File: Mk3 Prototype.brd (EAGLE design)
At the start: 113 x 53.5 mm, 133 parts, among them IC1 STM32F401R, IC2 CC3100, IC3 S25FL216K0PMFI011, J1 ZX62-AB-5PA(11), J2 SWD_SHROUD_SMD, J4 Arduino Headers, J7 SFV30R-2STE1HLF, Q1 BSS84W, Q10 2N7002KW, Q11 BSS84W, Q12 2N7002KW, U1 USD-SOCKETNEW, U2 JHD12864-G13BSW-OUTLINE, U3 MCP73831, X1 ABS07-32.768KHZ-T, X2 Q24FA20H00396, X3 CRYSTAL-3.2-2.5, X4 ABS07-32.768KHZ-T, Y1 AH316M245001-T

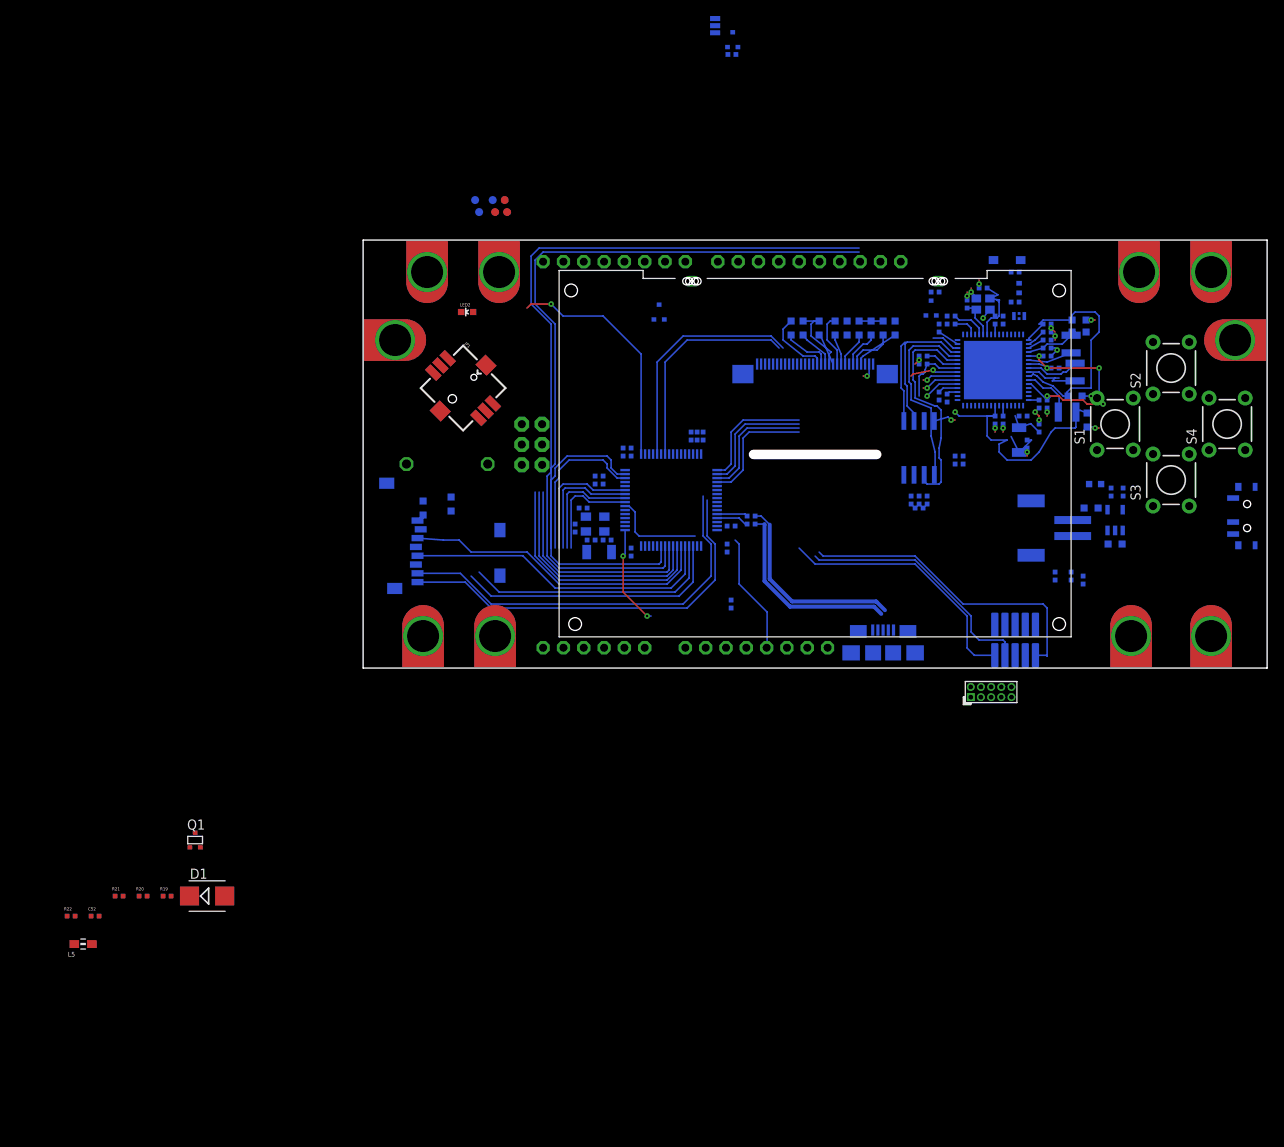
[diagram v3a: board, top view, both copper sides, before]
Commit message: starting stm32 100pin schematic
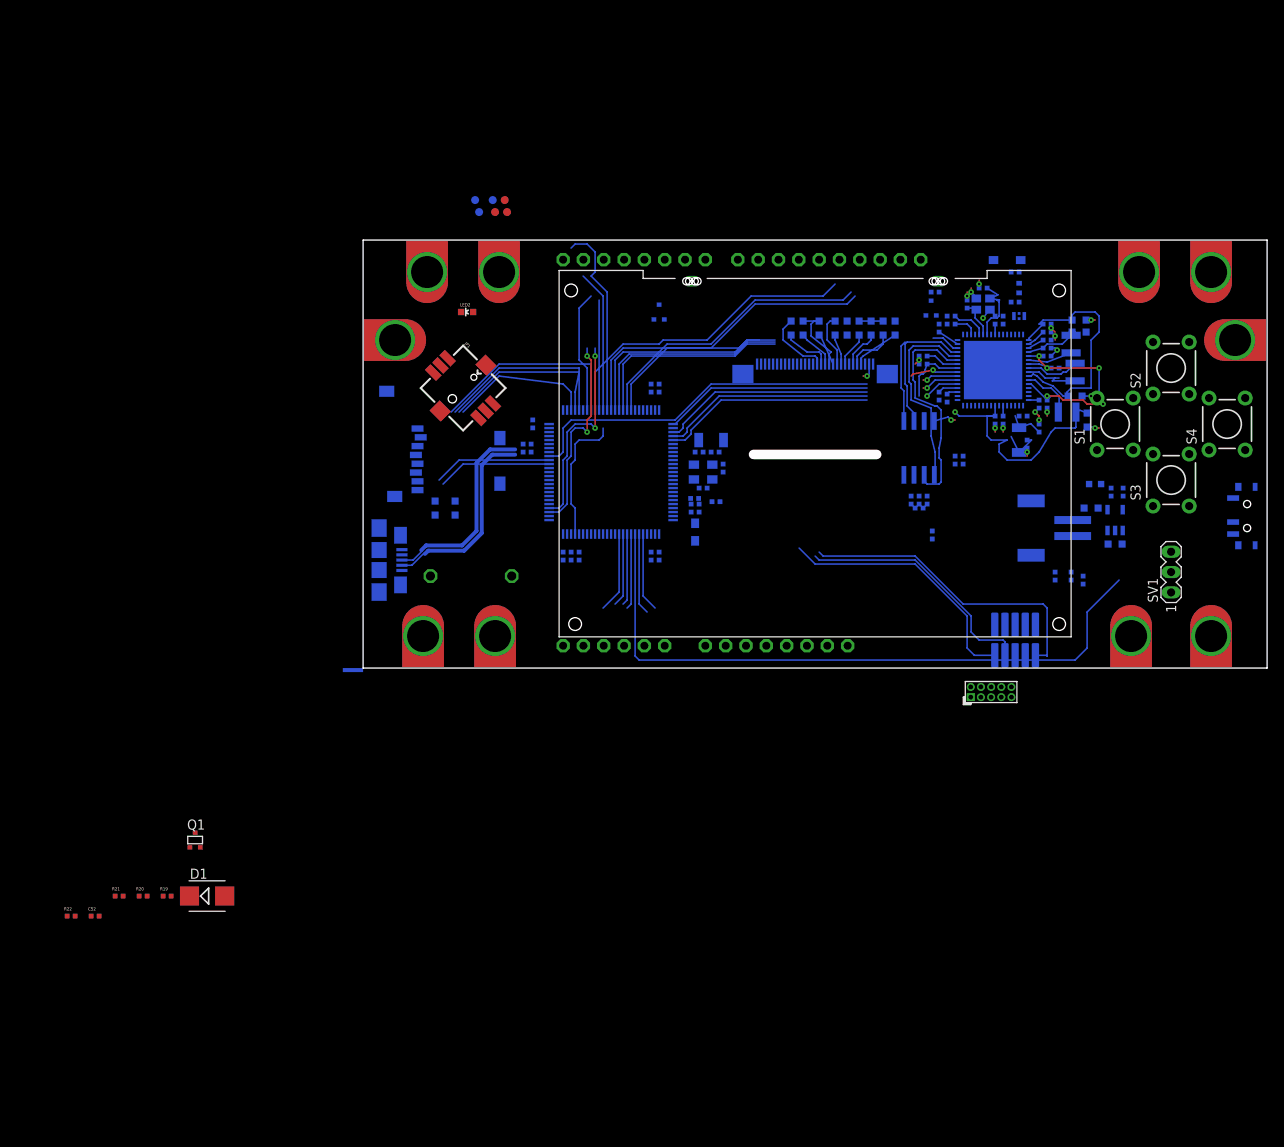
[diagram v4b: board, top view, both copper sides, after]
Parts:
- removed IC1: STM32F401R, TiLDA Mk3 Parts:LQFP64-10X10
- removed J4: Arduino Headers, TiLDA Mk3 Parts:ARDUINOR3-LWKTXT-REF-SPI
- removed Q10: 2N7002KW, TiLDA Mk3 Parts:SC70-3-R
- removed R42: 0402/10K/5%, TiLDA Mk3 Parts:R0402-SMALLER
- removed SJ3: ISP_RESET, TiLDA Mk3 Parts:SJ_3
- added C55: 0402/1u/10V/X5R, TiLDA Mk3 Parts:C0402-SMALLER
- added C56: 0402/100n/10V/X5R, TiLDA Mk3 Parts:C0402-SMALLER
- added IC4: STM32F401V, TiLDA Mk3 Parts:TQFP100
- added SV1: (no value), con-lstb:MA03-1
- added U4: ARDUINOR3-NODIM, TiLDA Mk3 Parts:ARDUINOR3-NODIM
- C49: value 0402/0R -> 0402/100n/10V/X5R
- moved L5 92.2 mm to (41.5, 17.0), flipped to the bottom, turned to 90 degrees
- moved J1 64.1 mm to (2.00, 13.5), turned to 180 degrees
- moved R16 29.7 mm to (20.5, 28.0), turned to 0 degrees
- moved R15 29.1 mm to (20.5, 27.0), turned to 0 degrees
- moved R14 26.6 mm to (71.1, 16.6)
- moved C7 23.0 mm to (25.0, 14.0), turned to 90 degrees
- moved C9 22.4 mm to (36.5, 35.5), turned to 180 degrees
- moved C10 20.5 mm to (27.0, 14.0)
- moved C48 20.3 mm to (26.0, 14.0), turned to 90 degrees
- moved C5 20.2 mm to (36.5, 34.5), turned to 180 degrees
- moved C35 20.0 mm to (45.0, 25.0)
- moved X4 19.8 mm to (43.5, 28.5)
- moved C53 19.0 mm to (44.0, 27.0), turned to 180 degrees
- moved C54 15.9 mm to (42.0, 27.0), turned to 180 degrees
- moved C36 15.2 mm to (42.5, 22.5), turned to 0 degrees
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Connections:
- removed net D10: J4.D10
- removed net D11: J4.D11
- removed net D12: J4.D12
- removed net D13: J4.D13
- removed net D5: J4.D5
- removed net D6: J4.D6
- removed net D9: J4.D9
- removed net ISP_!RESET: J4.!RESET@ISP, Q10.3, SJ3.1, SJ3.2
- removed net ISP_!RESET!_IO: Q10.1, R42.1
- removed net N$39: IC1.22
- removed net N$42: IC1.26
- removed net N$43: IC1.24
- removed net N$44: IC1.62
- removed net N$45: IC1.25
- removed net N$49: IC1.16
- removed net N$50: IC1.50
- removed net N$51: IC1.27
- removed net N$53: IC1.61
- removed net N$54: IC1.29
- removed net RX: J4.D0
- removed net SPI1_CLK: IC1.21, J7.13
- removed net SPI3_MISO: IC1.56, J4.MISO
- removed net TX: J4.D1
- removed net WIFI_CLK: IC1.34, IC2.5
- removed net WIFI_CS: IC1.33, IC2.8
- removed net WIFI_MISO: IC1.35, IC2.7
- removed net WIFI_MOSI: IC1.36, IC2.6
- new net SPI2_CLK: IC4.84, U4.D13
- new net SPI2_MISO: IC4.53, U4.D12
- new net SPI2_MOSI: IC4.54, U4.D11
- new net SPI4_MISO: IC2.7, IC4.4
- new net SPI4_MOSI: IC2.6, IC4.5
- new net SPI4_NSS: IC2.8, IC4.3
- new net SPI4_SCK: IC2.5, IC4.1
- new net TIM2_CH1: IC4.77, U4.D6
- new net TIM2_CH3: IC4.47, U4.D5
- new net TIM4_CH3: IC4.95, U4.D9
- new net TIM4_CH4: IC4.96, U4.D10
- new net USART2_RX: IC4.87, U4.D0
- new net USART2_TX: IC4.86, U4.D1
- net +3V3: now also C49.2, C56.2, IC4.100, IC4.11, IC4.19, IC4.28, IC4.50, IC4.75, U4.3V, U4.IOREF; no longer IC1.19, IC1.32, IC1.48, IC1.64, J4.3V, J4.IOREF
- net 5V0: now also U4.5V; no longer J4.5V, J4.5V@ISP
- net A0: now also IC4.30, U4.A0; no longer IC1.8, J4.A0
- net A1: now also IC4.31, U4.A1; no longer IC1.9, J4.A1
- net A2: now also IC4.33, U4.A2; no longer IC1.10, J4.A2
- net A3: now also IC4.34, U4.A3; no longer IC1.11, J4.A3
- net A4: now also IC4.35, U4.A4; no longer IC1.14, J4.A4
- net A5: now also IC4.36, U4.A5; no longer IC1.15, J4.A5
- net ADC3: now also IC4.26; no longer IC1.17
- net AREF: now also U4.AREF; no longer J4.AREF
- net BOOT0: now also IC4.94; no longer IC1.60
- net D2: now also IC4.82, U4.D2; no longer J4.D2
- net D3: now also U4.D3; no longer J4.D3
- net D4: now also IC4.85, U4.D4; no longer J4.D4
- net D7: now also IC4.98, U4.D7; no longer J4.D7
- net D8: now also IC4.97, U4.D8; no longer J4.D8
- net D_N: now also IC4.70; no longer IC1.44
- net D_P: now also IC4.71; no longer IC1.45
- net GND: now also C55.1, C56.1, IC4.10, IC4.20, IC4.27, IC4.74, IC4.99, U4.GND, U4.GND1, U4.GND2; no longer IC1.12, IC1.18, IC1.63, J4.GND@1, J4.GND@2, J4.GND@3, J4.GND@ISP, Q10.2, R42.2
- net I2C_SCL: now also IC4.92, U4.SCL; no longer IC1.58, J4.SCL
- net I2C_SDA: now also IC4.93, U4.SDA; no longer IC1.59, J4.SDA
- net LCD_!CS: now also IC4.90
- net LCD_A0: now also IC4.88
- net MASTER_RESET: now also U4.RESET; no longer J4.!RESET, SJ3.3
- net MCO1: now also IC4.67; no longer IC1.41
- net N$13: now also IC4.21, IC4.22; no longer IC1.13
- net N$30: now also IC4.69; no longer IC1.43
- net N$31: now also IC4.12; no longer IC1.5
- net N$32: now also IC4.68; no longer IC1.42
- net N$33: now also IC4.13; no longer IC1.6
- net N$37: now also IC4.49; no longer IC1.47
- net N$38: now also C55.2, IC4.73; no longer C49.2, IC1.31
- net N$4: now also IC4.48; no longer IC1.30
- net N$48: now also IC4.29; no longer IC1.20
- net N$52: now also IC4.37; no longer IC1.28
- net N$55: now also IC4.63; no longer IC1.37
- net N$56: now also IC4.64; no longer IC1.38
- net NRST: now also IC4.14; no longer IC1.7
- net OCS32_IN: now also IC4.8; no longer IC1.3
- net OCS32_OUT: now also IC4.9; no longer IC1.4
- net SDIO_CLK: now also IC4.80; no longer IC1.53
- net SDIO_CMD: now also IC4.83; no longer IC1.54
- net SDIO_D0: now also IC4.65; no longer IC1.39
- net SDIO_D1: now also IC4.66; no longer IC1.40
- net SDIO_D2: now also IC4.78; no longer IC1.51
- net SDIO_D3: now also IC4.79; no longer IC1.52
- net SDIO_SW: now also IC4.7; no longer IC1.2
- net SPI1_MOSI: now also IC4.32, SV1.2; no longer IC1.23, J7.14
- net SPI3_MOSI: now also IC4.91, J7.14; no longer IC1.57, J4.MOSI
- net SPI3_SCK: now also IC4.89, J7.13; no longer IC1.55, J4.SCK
- net SWCLK: now also IC4.76; no longer IC1.49
- net SWDAT: now also IC4.72; no longer IC1.46
- net VBATT_IN: now also IC4.6; no longer IC1.1
- net VIN: now also U4.VIN; no longer J4.VIN
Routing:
- net I2C_SCL: track 98.1 -> 36.0 mm
- net I2C_SDA: track 95.4 -> 35.8 mm
- net SPI1_MOSI: track 27.3 -> 82.7 mm
- net MCO1: track 0.00 -> 45.2 mm
- net SPI2_CLK: track 0.00 -> 39.3 mm
- net SDIO_D0: track 50.2 -> 14.3 mm
- net SDIO_D1: track 50.4 -> 14.8 mm
- net SPI4_NSS: track 0.00 -> 32.7 mm, vias 0 -> 1
- net SPI4_MOSI: track 0.00 -> 31.3 mm, vias 0 -> 1
- net SPI4_MISO: track 0.00 -> 31.1 mm, vias 0 -> 1
- net SPI4_SCK: track 0.00 -> 30.5 mm, vias 0 -> 1
- net ADC3: track 29.5 -> 0.00 mm, vias 1 -> 0
- net SPI1_CLK: track 29.2 -> 0.00 mm
- net SPI3_MISO: track 29.1 -> 0.00 mm
- net LCD_!CS: track 0.00 -> 26.4 mm
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
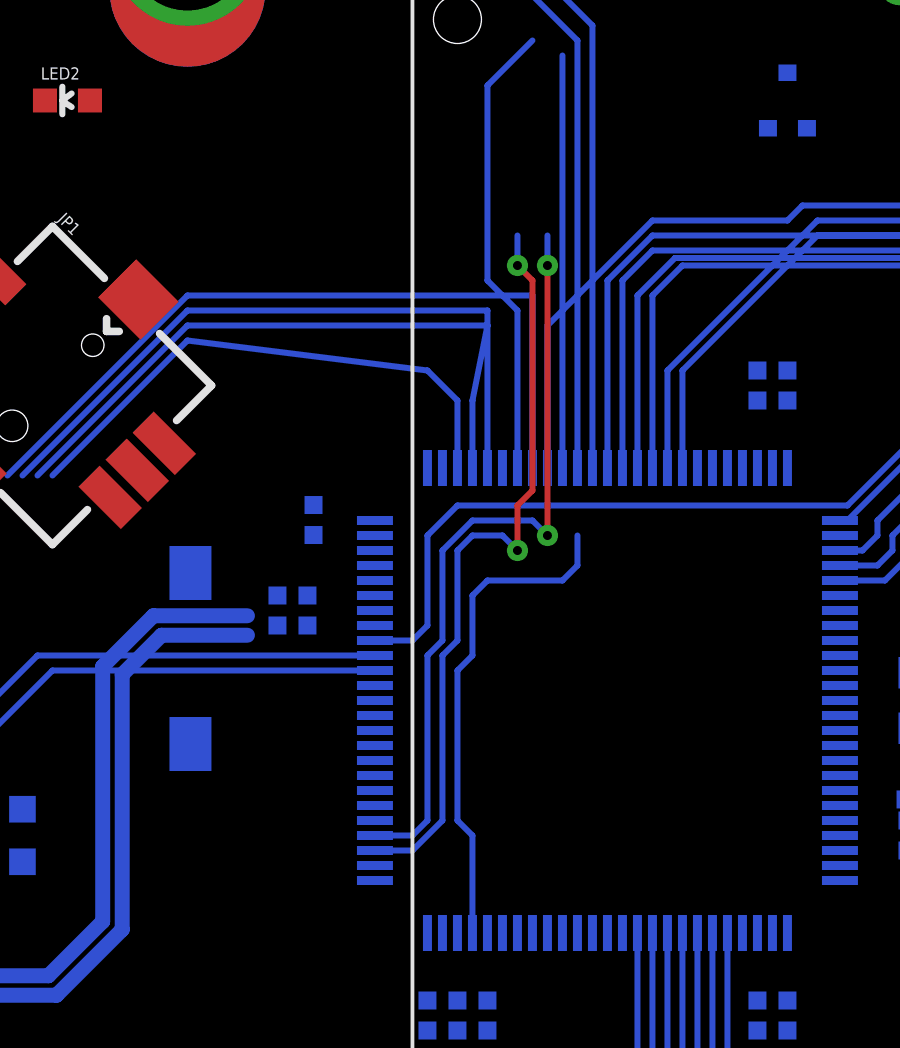
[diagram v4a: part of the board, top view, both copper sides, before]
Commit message: arduino gpio wired
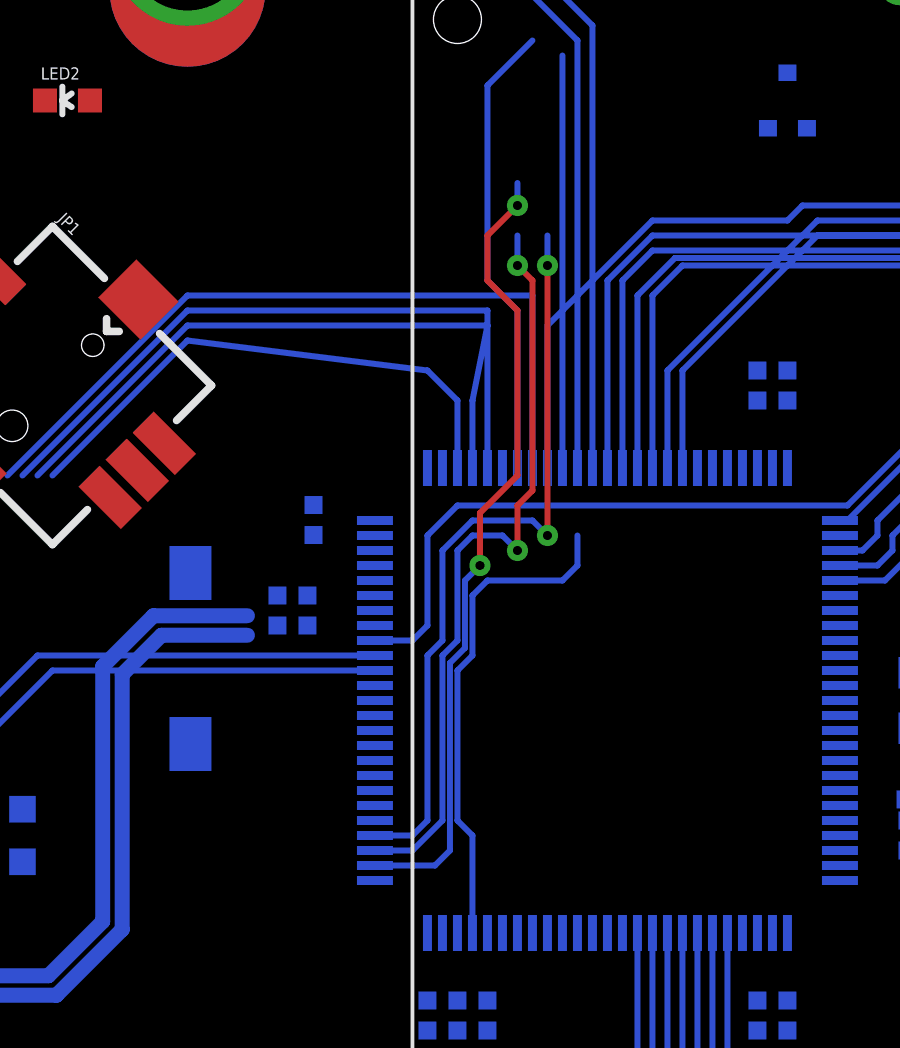
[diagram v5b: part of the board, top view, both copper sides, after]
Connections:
- removed net D3: U4.D3
- new net TIM1_CH1N: IC4.52, U4.D3
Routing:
- net TIM1_CH1N: track 0.00 -> 26.7 mm, vias 0 -> 2
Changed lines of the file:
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@@
 <wire x1="28.5" y1="46.5" x2="30.08" y2="51.05" width="0" layer="19" extent="1-16"/>
-</signal>
-<signal name="D3">
-<contactref element="U4" pad="D3"/>
 </signal>
 <signal name="D4">
@@
 <wire x1="26" y1="52.5" x2="25" y2="51.05" width="0" layer="19" extent="16-16"/>
 </signal>
+<signal name="TIM1_CH1N">
+<contactref element="IC4" pad="52"/>
+<contactref element="U4" pad="D3"/>
+<wire x1="23.25" y1="19" x2="25.25" y2="19" width="0.2" layer="16"/>
+<wire x1="25.25" y1="19" x2="25.75" y2="19.5" width="0.2" layer="16"/>
+<wire x1="25.75" y1="19.5" x2="25.75" y2="25.75" width="0.2" layer="16"/>
+<wire x1="25.75" y1="25.75" x2="26.25" y2="26.25" width="0.2" layer="16"/>
+<wire x1="26.25" y1="26.25" x2="26.25" y2="28.5" width="0.2" layer="16"/>
+<wire x1="26.25" y1="28.5" x2="26.75" y2="29" width="0.2" layer="16"/>
+<via x="26.75" y="29" extent="1-16" drill="0.3" shape="octagon"/>
+<wire x1="26.75" y1="29" x2="26.75" y2="30.75" width="0.2" layer="1"/>
+<wire x1="26.75" y1="30.75" x2="28" y2="32" width="0.2" layer="1"/>
+<wire x1="28" y1="32" x2="28" y2="37.5" width="0.2" layer="1"/>
+<wire x1="28" y1="37.5" x2="27" y2="38.5" width="0.2" layer="1"/>
+<wire x1="27" y1="38.5" x2="27" y2="40" width="0.2" layer="1"/>
+<wire x1="27" y1="40" x2="28" y2="41" width="0.2" layer="1"/>
+<via x="28" y="41" extent="1-16" drill="0.3" shape="octagon"/>
+<wire x1="28" y1="41" x2="28" y2="41.75" width="0.2" layer="16"/>
+<wire x1="28" y1="41.75" x2="32.62" y2="51.05" width="0" layer="19" extent="1-16"/>
+</signal>
 </signals>
